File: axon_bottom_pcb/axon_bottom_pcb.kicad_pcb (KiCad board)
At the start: 2 copper layers, 227.6 x 99.2 mm, 18 parts

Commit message: fixed libraries, final pcb version
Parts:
- removed the REF** at (215.3, 50.8)
- removed the REF** at (198.1, 62.9)
- removed the REF** at (11.4, 62.9)
- removed the REF** at (11.4, 50.8)
- removed the REF** at (-5.71, 50.8)
- removed the REF** at (198.1, 50.8)
- moved REF** 0.90 mm to (-5.08, 62.2)
- moved REF** 0.90 mm to (-5.08, -29.2)
- moved REF** 0.90 mm to (214.6, 62.2)
- moved REF** 0.90 mm to (214.6, -29.2)
- moved REF** 0.63 mm to (-5.08, -12.7)
- moved REF** 0.63 mm to (214.6, -12.7)

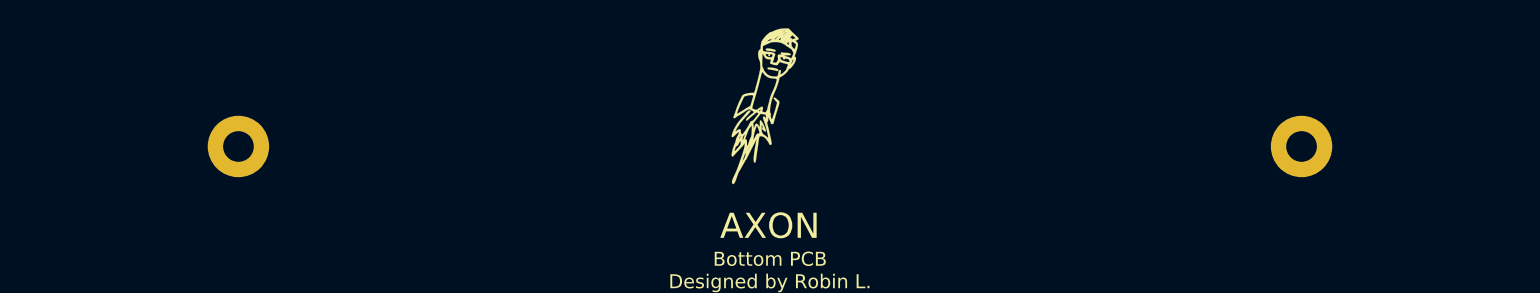
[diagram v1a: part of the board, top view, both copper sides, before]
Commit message: board updates to fix 1.0 issues
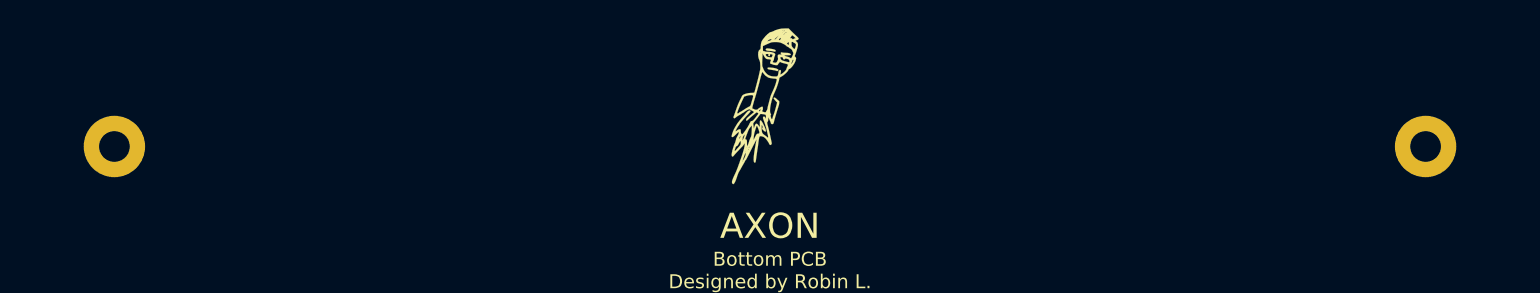
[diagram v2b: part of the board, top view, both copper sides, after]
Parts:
- moved REF** 8.89 mm to (57.8, 47.6)
- moved REF** 8.89 mm to (151.8, 47.6)

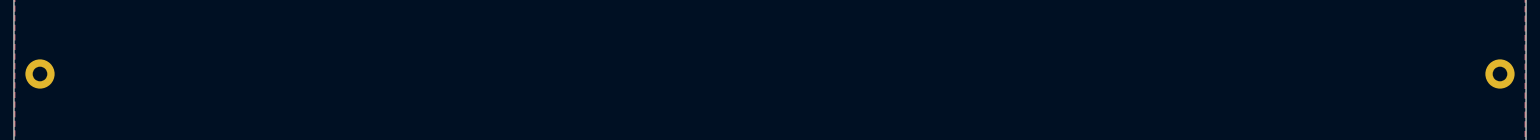
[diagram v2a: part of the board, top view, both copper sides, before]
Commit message: updated bottom pcb with v2 screw holes
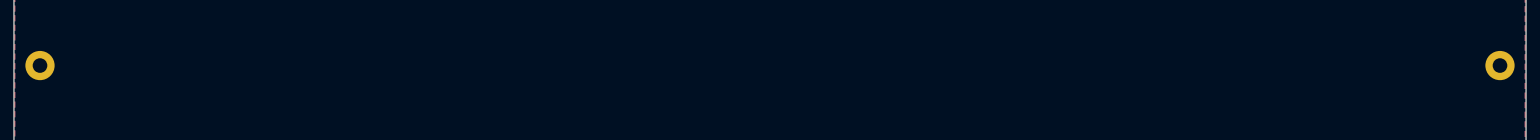
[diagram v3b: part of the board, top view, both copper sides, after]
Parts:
- moved REF** 1.27 mm to (214.6, -14.0)
- moved REF** 1.27 mm to (-5.08, -14.0)

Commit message: update bottom pcb
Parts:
- removed the REF** at (142.9, 4.45)
- removed the REF** at (66.7, 4.45)
- added REF**: MountingHole_2.2mm_M2_Pad, MountingHole:MountingHole_2.2mm_M2_Pad, F.Cu at (104.8, 0.00)
- moved REF** 20.8 mm to (66.0, 28.6)
- moved REF** 20.8 mm to (143.5, 28.6)

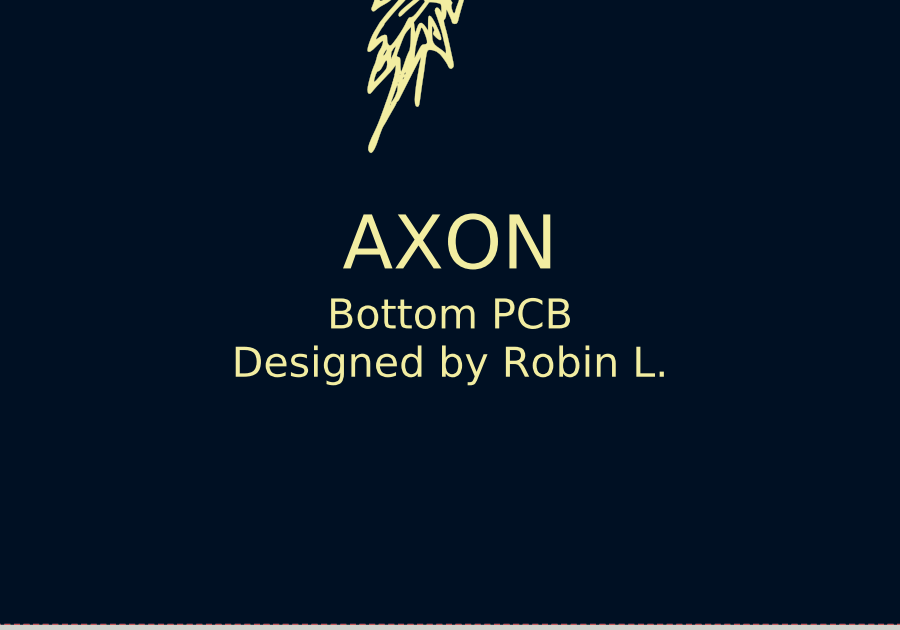
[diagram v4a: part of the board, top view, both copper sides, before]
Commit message: add dimensions to pcb editor
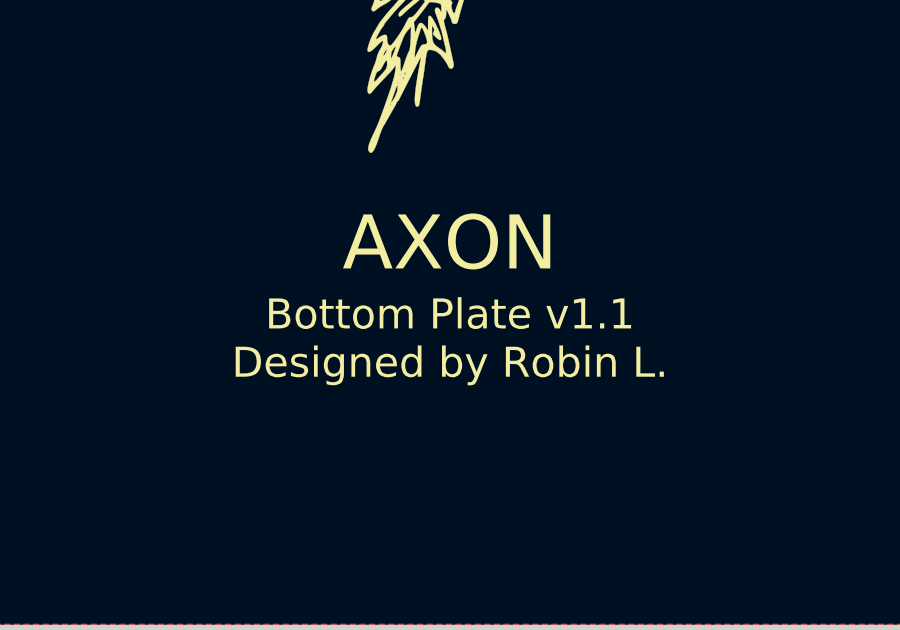
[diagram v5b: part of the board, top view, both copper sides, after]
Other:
- board text added: "Bottom Plate v1.1 Designed by Robin L."
- board text removed: "Bottom PCB Designed by Robin L."
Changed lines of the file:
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@@
   (general
     (thickness 1.6)
-    (drawings 274)
+    (drawings 288)
     (tracks 0)
     (zones 0)
@@
     (40 Dwgs.User user)
     (41 Cmts.User user)
-    (42 Eco1.User user)
+    (42 Eco1.User user hide)
     (43 Eco2.User user)
     (44 Edge.Cuts user)
@@
     (visible_elements 7EFFFFFF)
     (pcbplotparams
-      (layerselection 0x010fc_ffffffff)
+      (layerselection 0x010f0_ffffffff)
       (usegerberextensions false)
-      (usegerberattributes true)
+      (usegerberattributes false)
       (usegerberadvancedattributes true)
       (creategerberjobfile true)
@@
       (effects (font (size 1 1) (thickness 0.15)))
     )
-    (fp_text user %R (at 0.3 0) (layer F.Fab)
-      (effects (font (size 1 1) (thickness 0.15)))
-    )
     (fp_circle (center 0 0) (end 2.45 0) (layer F.CrtYd) (width 0.05))
     (fp_circle (center 0 0) (end 2.2 0) (layer Cmts.User) (width 0.15))
+    (fp_text user %R (at 0.3 0) (layer F.Fab)
+      (effects (font (size 1 1) (thickness 0.15)))
+    )
     (pad 1 thru_hole circle (at 0 0) (size 4.4 4.4) (drill 2.2) (layers *.Cu *.Mask))
   )
@@
     (pad 1 thru_hole circle (at 0 0) (size 4.4 4.4) (drill 2.2) (layers *.Cu *.Mask))
   )
+  (dimension 99.170159 (width 0.15) (layer Dwgs.User)
+    (gr_text "99.170 mm" (at -21.239 16.565079 90) (layer Dwgs.User)
+      (effects (font (size 1 1) (thickness 0.15)))
+    )
+    (feature1 (pts (xy -6 -33.02) (xy -20.525421 -33.02)))
+    (feature2 (pts (xy -6 66.150159) (xy -20.525421 66.150159)))
+    (crossbar (pts (xy -19.939 66.150159) (xy -19.939 -33.02)))
+    (arrow1a (pts (xy -19.939 -33.02) (xy -19.352579 -31.893496)))
+    (arrow1b (pts (xy -19.939 -33.02) (xy -20.525421 -31.893496)))
+    (arrow2a (pts (xy -19.939 66.150159) (xy -19.352579 65.023655)))
+    (arrow2b (pts (xy -19.939 66.150159) (xy -20.525421 65.023655)))
+  )
+  (dimension 227.550349 (width 0.15) (layer Dwgs.User)
+    (gr_text "227.550 mm" (at 104.775174 74.198) (layer Dwgs.User)
+      (effects (font (size 1 1) (thickness 0.15)))
+    )
+    (feature1 (pts (xy -9 63.150159) (xy -9 73.484421)))
+    (feature2 (pts (xy 218.550349 63.150159) (xy 218.550349 73.484421)))
+    (crossbar (pts (xy 218.550349 72.898) (xy -9 72.898)))
+    (arrow1a (pts (xy -9 72.898) (xy -7.873496 72.311579)))
+    (arrow1b (pts (xy -9 72.898) (xy -7.873496 73.484421)))
+    (arrow2a (pts (xy 218.550349 72.898) (xy 217.423845 72.311579)))
+    (arrow2b (pts (xy 218.550349 72.898) (xy 217.423845 73.484421)))
+  )
+  (gr_circle (center 214.630349 -13.97005) (end 215.730349 -13.97005) (layer Eco1.User) (width 0.2))
+  (gr_circle (center 214.630349 -29.209999) (end 215.730349 -29.209999) (layer Eco1.User) (width 0.2))
+  (gr_circle (center -5.08 -29.21) (end -3.98 -29.21) (layer Eco1.User) (width 0.2))
+  (gr_circle (center -5.079999 -13.970049) (end -3.979999 -13.970049) (layer Eco1.User) (width 0.2))
+  (gr_arc (start 215.550349 -30.019999) (end 218.550349 -30.019999) (angle -90) (layer Eco1.User) (width 0.2))
+  (gr_line (start 218.550349 -13.050049) (end 218.550349 -30.019999) (layer Eco1.User) (width 0.2))
+  (gr_arc (start 215.550349 -13.050049) (end 215.550349 -10.05005) (angle -90) (layer Eco1.User) (width 0.2))
+  (gr_line (start -6 -10.05005) (end 215.550349 -10.05005) (layer Eco1.User) (width 0.2))
+  (gr_arc (start -6 -13.05005) (end -9 -13.05005) (angle -90) (layer Eco1.User) (width 0.2))
+  (gr_line (start -9 -30.02) (end -9 -13.05005) (layer Eco1.User) (width 0.2))
+  (gr_arc (start -5.999999 -30.02) (end -6 -33.02) (angle -90) (layer Eco1.User) (width 0.2))
+  (gr_line (start 215.550349 -33.02) (end -6 -33.02) (layer Eco1.User) (width 0.2))
   (gr_circle (center 104.775174 0) (end 107.300524 0) (layer Eco1.User) (width 0.2))
   (gr_line (start 104.775174 0) (end 143.510349 28.575) (layer Eco1.User) (width 0.2))
@@
   (gr_line (start 104.775174 -33.02) (end 104.775174 66.150159) (layer Eco1.User) (width 0.2))
   (gr_line (start 218.550349 16.565079) (end -9 16.565079) (layer Eco1.User) (width 0.2))
-  (gr_text "Bottom PCB\nDesigned by Robin L." (at 104.775 56.515) (layer F.SilkS)
+  (gr_text "Bottom Plate v1.1\nDesigned by Robin L." (at 104.775 56.515) (layer F.SilkS)
     (effects (font (size 1 1) (thickness 0.15)))
   )

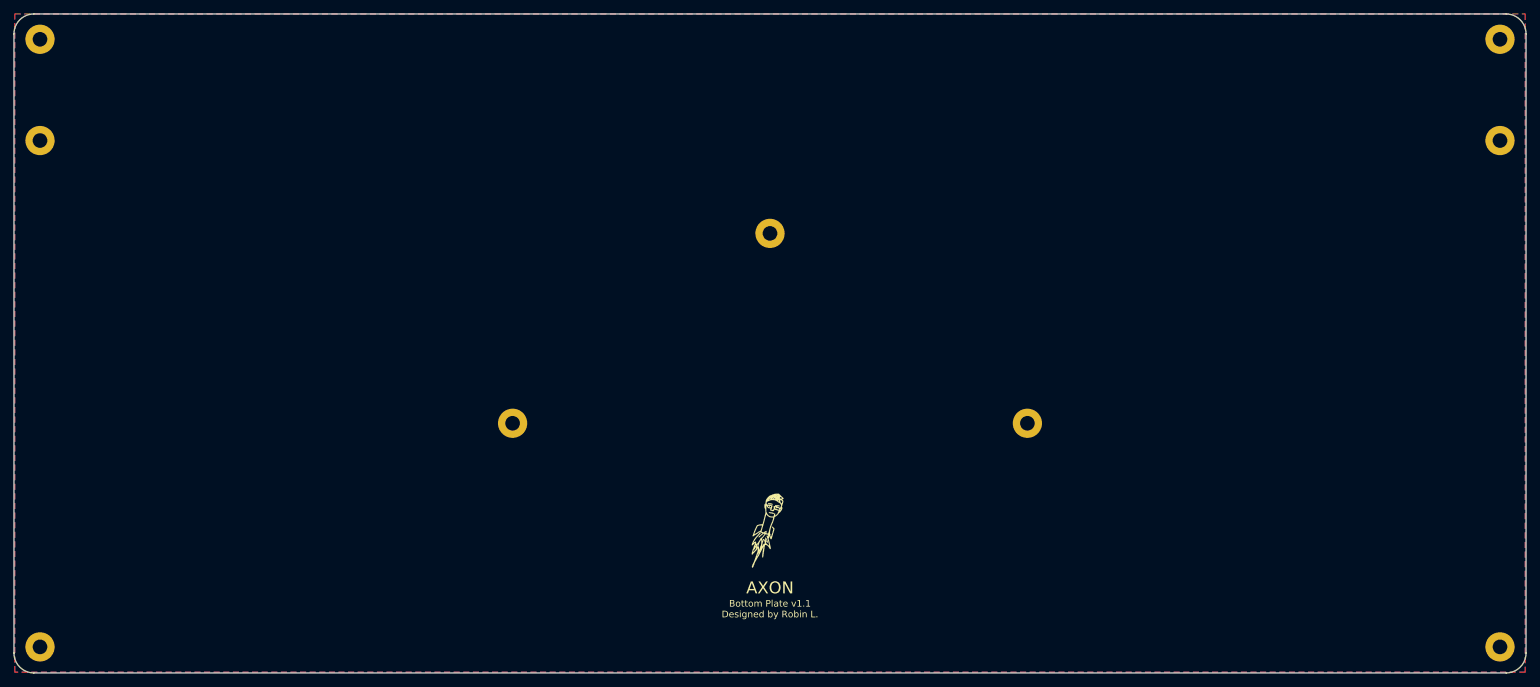
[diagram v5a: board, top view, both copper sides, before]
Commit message: update rear pcb outline
and updated .gitignore while I was at it.
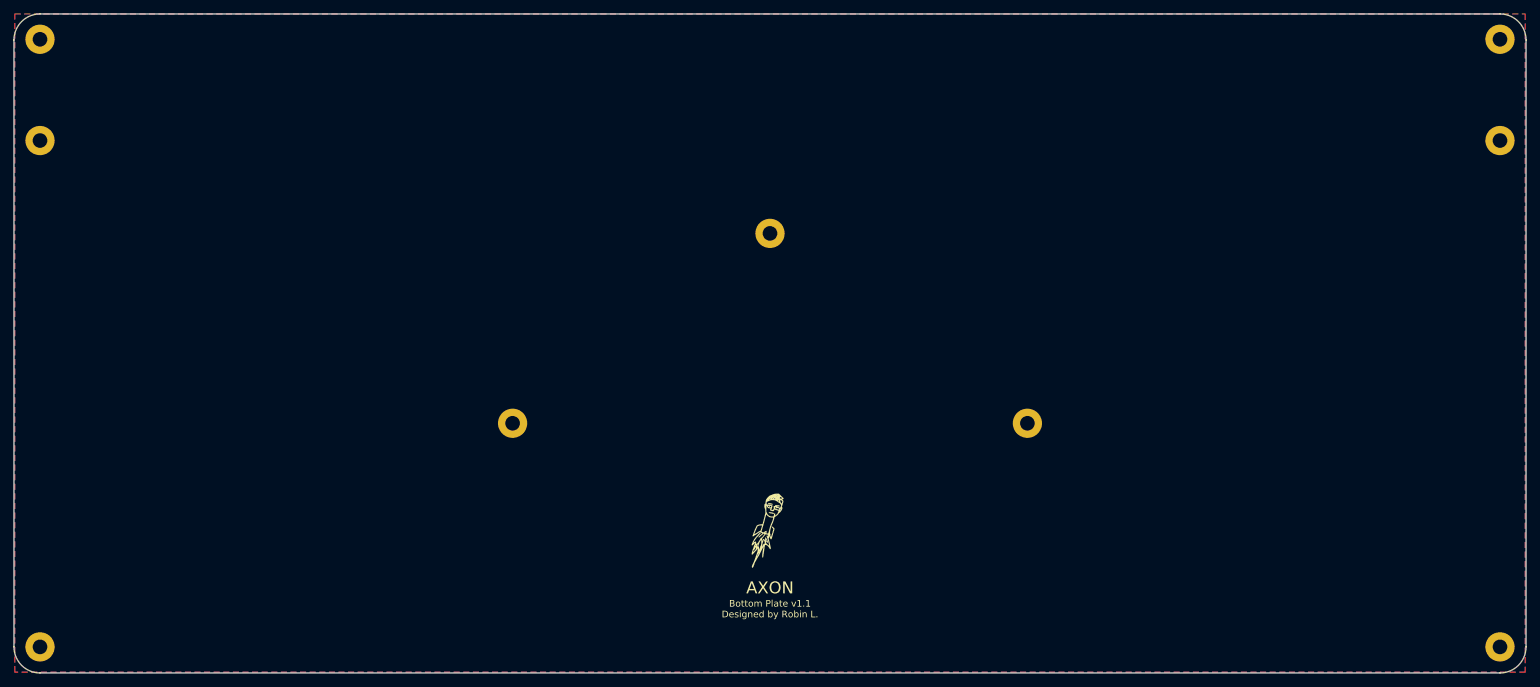
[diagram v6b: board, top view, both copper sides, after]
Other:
- outline, holes or cut-outs redrawn
- net class Default removed
